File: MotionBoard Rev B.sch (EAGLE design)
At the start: 86 parts, among them IC1 LPC1769, IC2 LD1117, Q1 BSL207SP, Q2 12MHz, Q3 25MHz, U1 ARDUINO-FIREPICK+RAMPS, X1 ST9S008V4AR1500

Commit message: Update board files
Signed-off-by: Paul Jones <paul@pauljones.id.au>
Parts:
- removed C45, C50, C64: 10uF, SparkFun:CAP_POL1206
- removed C48: 1uF, SparkFun:CAP_POL1206
- removed JP4: MICRO-USB-FCI-10103592, micro-usb-fci-10103592:MICRO-USB-FCI-10103592
- removed S1, S2, S3, S4: (no value), SparkFun:TAC_SWITCHSMD
- added C10, C17, C18: 1u, iwt:CAP0603
- added C16: 100n, iwt:CAP0603
- added C19, C20, C6, C7: 10u, iwt:CAP0603
- added DFU: SW3, iwt:TOGGLE-SW-SMD
- added ISP: SW2, iwt:TOGGLE-SW-SMD
- added RST: SW1, iwt:TOGGLE-SW-SMD
- added X2: USB-MICRO-B, iwt:USB-MICRO-B
- C1, C15, C44, C46, C51, C52, C53: value .1uF -> 100n; device resistor:C-EUC0603 -> iwt:CAP0603
- C11: value .1uF -> 100n
- C12, C13, C14, C8: value .1uF -> 100n; device rcl:C-EUC0603 -> iwt:CAP0603
- C2, C3, C4, C5: value 18pF -> 18p; device rcl:C-EUC0603 -> iwt:CAP0603
- C49: value 470pF -> 470p; device resistor:C-EUC0603K -> iwt:CAP0603
- C54, C55, C56, C57, C58, C59: value 18pF -> 18p; device resistor:C-EUC0603 -> iwt:CAP0603
- C9: value 10uF -> 100n; device SparkFun:CAP_POL1206 -> iwt:CAP0603
- D1: value DIODE-SMB -> MBR0530; device iwt:DIODE-ZENER -> SparkFun-DiscreteSemi:DIODESOD123
- IC1: value LPC1769 -> LPC1769FBD100 or LPC4078FBD100E; device microbuilder:LPC1768 -> iwt:LPC1768
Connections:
- removed net N$61: JP4.D+, R8.1
- removed net N$62: JP4.D-, R9.1
- new net D_N: R9.1, X2.D_N
- new net D_P: R8.1, X2.D_P
- net !RST: now also RST.I; no longer S1.1, S1.2, S3.1, S3.2
- net 3.3V: now also C19.1, C20.1, C7.1, C9.1, IC1.N.C., IC1.VDD(3V3), IC1.VDD(REG)(3V3); no longer C50.+, C9.+, IC1.VDD(3V3)1, IC1.VDD(3V3)2, IC1.VDD(3V3)3, IC1.VDD(3V3)4, IC1.VDD(REG)(3V3)1, IC1.VDD(REG)(3V3)2
- net 5V: now also C16.1, C17.1, C18.1; no longer C64.+
- net GND: now also C10.2, C16.2, C17.2, C18.2, C19.2, C20.2, C6.2, C7.2, C9.2, DFU.C, DFU.GND, IC1.VSS, ISP.C, ISP.GND, RST.C, RST.GND, X2.GND, X2.SHIELD; no longer C45.-, C48.-, C50.-, C64.-, C9.-, IC1.VSS2, IC1.VSS3, IC1.VSS4, IC1.VSS5, IC1.VSS6, JP4.GND, S1.3, S1.4, S2.3, S2.4, S3.3, S3.4, S4.3, S4.4
- net N$12: now also C10.1; no longer C48.+
- net N$9: now also X2.VCC; no longer JP4.VCC
- net P2[10]: now also ISP.I; no longer S2.1, S2.2, S4.1, S4.2
- net P2[12]: now also DFU.I
- net VDD: now also C6.1; no longer C45.+
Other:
- moved on the sheet: PTC1, R4, R5

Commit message: Cosmetic changes
Add new name to schematic and rearrange page 1 so it all fits on the
page
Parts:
- removed LOGO4: LOGO-FIREPICKMEDIUM, FirePick:LOGO-FIREPICKMEDIUM
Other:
- note added: "MotionBoard - for FirePick Delta (Smoothie and Ramps 1.4 Compatible)"
- note removed: "EARM01 CPU Module for FirePick Delta (Smoothie Compatible)"
- moved on the sheet: C11, C12, C13, C14, C15, C2, C3, C4, C5, IC1, L1, PTC1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

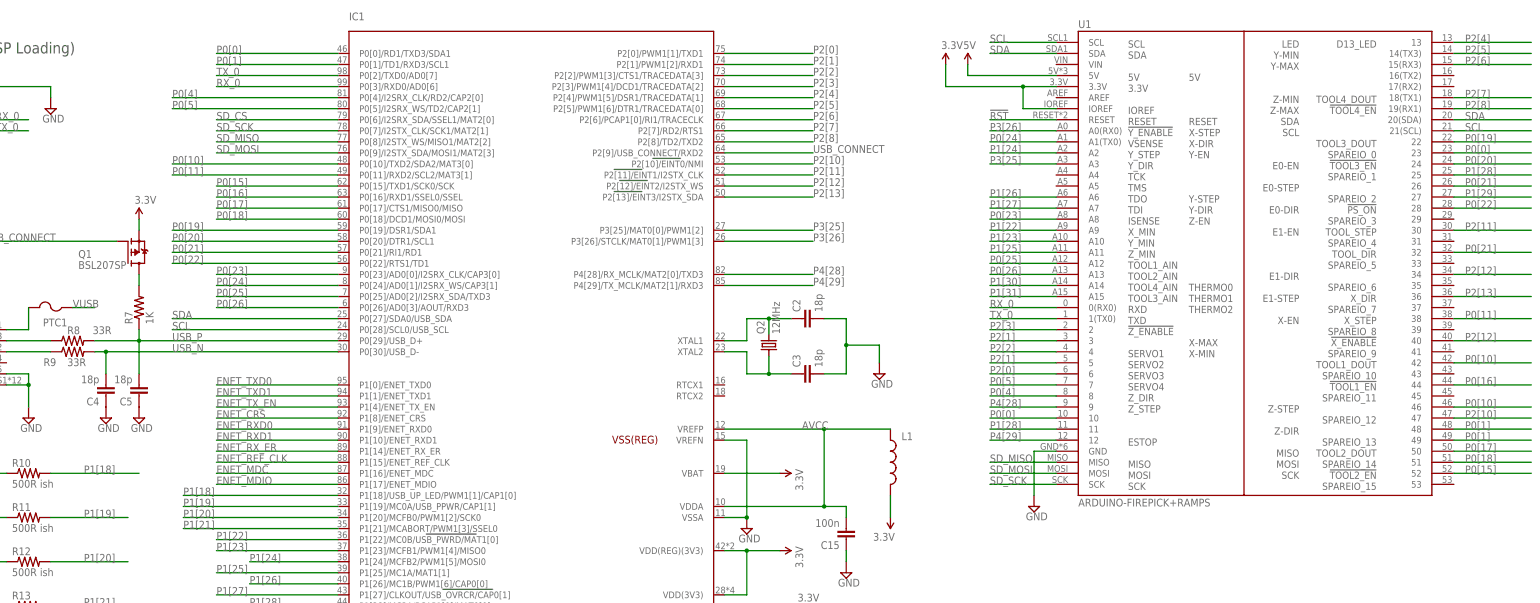
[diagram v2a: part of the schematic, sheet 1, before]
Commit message: Update with production files
Also note a "whoopsie" where wire jumpers are required...
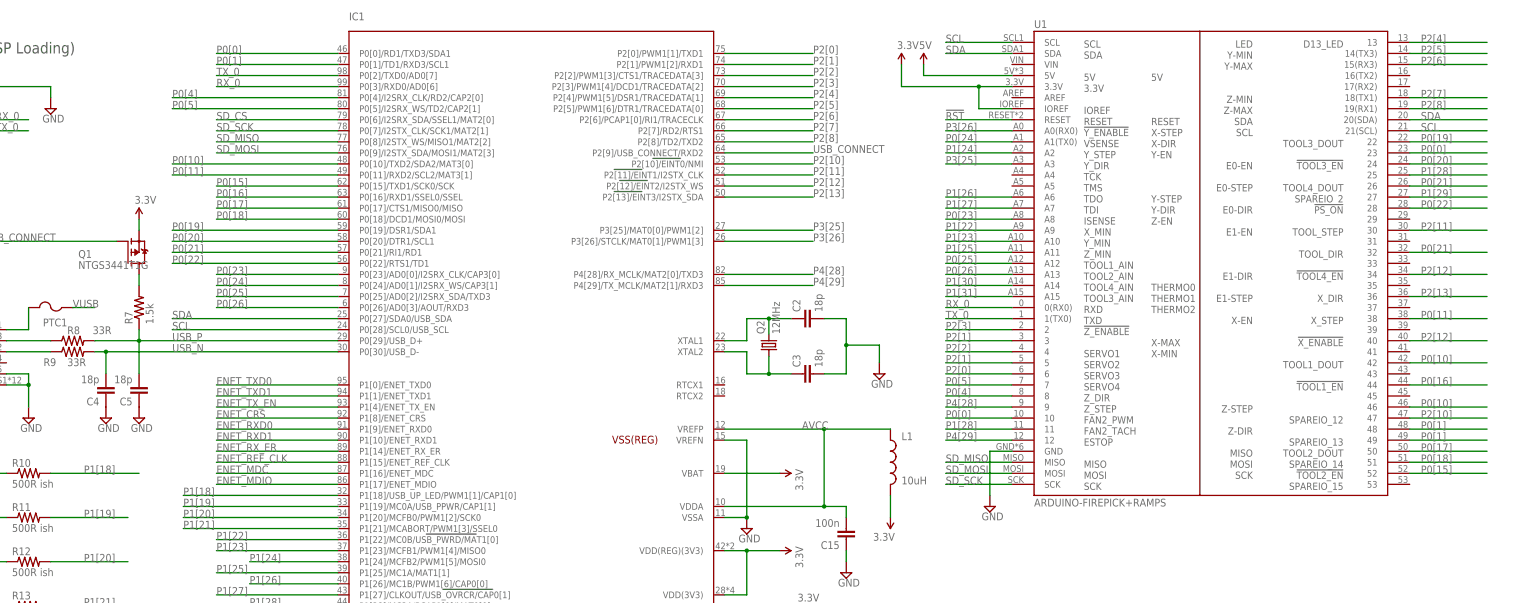
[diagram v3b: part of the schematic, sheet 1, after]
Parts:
- C11: device rcl:C-EUC0603 -> iwt:CAP0603
- L1: value (none) -> 10uH
- Q1: value BSL207SP -> NTGS3441T1G
- R51, R58, R59, R60: value 22R -> 33R
- R52: value 1.5K -> 1.5k
- R53, R62: value 10K -> 10k
- R63: value 12.1K -> 12.1k
- R7: value 1K -> 1.5k
- U1: device EARM01:ARDUINO-FIREPICK+RAMPS -> iwt:ARDUINO-FIREPICK+RAMPS
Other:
- note added: "P1[29]"
- note added: "P2[10]"
- note added: "Solder jumper wire"
